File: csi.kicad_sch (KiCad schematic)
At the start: 20 parts, among them J601 Conn_FFC_WE_68712614522_ONE-S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, U601 AP22615A_TSOT26, U602 AP22615A_TSOT26

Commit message: [#53901] Update symbols & footprints from lib
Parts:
- D601, D602: footprint antmicro-footprints:LED_0603_1608Metric_R -> antmicro-footprints:LED_0603_1608Metric_G; symbol antmicroLEDIndicationDiscrete:LED_R_0603_598-8D80-107F -> antmicroLEDIndicationDiscrete:LED_G_0603_598-8D80-107F
- J601: value Conn_FFC_WE_68712614522_ONE-SIDE -> Conn_FFC_WE_68715014522
- TP601, TP602: now left out of the parts list
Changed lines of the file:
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@@
   (title_block
     (title "CM4 Baseboard")
-    (date "2024-03-14")
+    (date "2024-03-22")
     (rev "1.0.0")
     (company "Antmicro")
@@
     )
   )
-  (symbol (lib_id "antmicroLEDIndicationDiscrete:LED_R_0603_598-8D80-107F") (at 152.4 181.61 270) (unit 1)
+  (symbol (lib_id "antmicroLEDIndicationDiscrete:LED_G_0603_598-8D80-107F") (at 152.4 181.61 270) (unit 1)
     (in_bom yes) (on_board yes) (dnp no) (fields_autoplaced)
-    (property "Reference" "D602" (at 157.48 184.4674 90)
+    (property "Reference" "D602" (at 157.48 184.4675 90)
       (effects (font (size 1.27 1.27) (thickness 0.15)) (justify left))
     )
-    (property "Value" "LED_G" (at 157.48 187.0074 90)
+    (property "Value" "LED_G" (at 157.48 187.0075 90)
       (effects (font (size 1.27 1.27) (thickness 0.15)) (justify left))
     )
-    (property "Footprint" "antmicro-footprints:LED_0603_1608Metric_R" (at 144.78 204.47 0)
+    (property "Footprint" "antmicro-footprints:LED_0603_1608Metric_G" (at 144.78 204.47 0)
       (effects (font (size 1.27 1.27) (thickness 0.15)) (justify left bottom) hide)
     )
@@
       (effects (font (size 1.27 1.27) (thickness 0.15)) (justify left bottom) hide)
     )
-    (property "MPN" "598-8D80-107F" (at 157.48 187.0074 90)
-      (effects (font (size 1.27 1.27) (thickness 0.15)) (justify left) hide)
+    (property "MPN" "598-8D80-107F" (at 139.7 204.47 0)
+      (effects (font (size 1.27 1.27) (thickness 0.15)) (justify left bottom) hide)
     )
     (property "Manufacturer" "Dialight" (at 137.16 204.47 0)
@@
     )
     (property "Value" "PESD5Z5_0F" (at 275.59 191.4525 90)
-      (effects (font (size 1.27 1.27) (thickness 0.15)) (justify left))
+      (effects (font (size 1.27 1.27) (thickness 0.15)) (justify left) hide)
     )
     (property "Footprint" "antmicro-footprints:SOD-523" (at 283.21 179.07 0)
@@
       (effects (font (size 1.27 1.27) (thickness 0.15)) (justify left bottom) hide)
     )
-    (property "MPN" "PESD5Z5.0F" (at 290.83 179.07 0)
-      (effects (font (size 1.27 1.27) (thickness 0.15)) (justify left bottom) hide)
+    (property "MPN" "PESD5Z5.0F" (at 275.59 191.4525 90)
+      (effects (font (size 1.27 1.27) (thickness 0.15)) (justify left))
     )
     (property "Author" "Antmicro" (at 293.37 179.07 0)
@@
   )
   (symbol (lib_id "antmicroFCCConnectors:Conn_FFC_WE_68715014522") (at 318.77 62.23 0) (unit 1)
-    (in_bom yes) (on_board yes) (dnp no) (fields_autoplaced)
-    (property "Reference" "J601" (at 323.85 59.69 0)
+    (in_bom yes) (on_board yes) (dnp no)
+    (property "Reference" "J601" (at 318.77 55.88 0)
       (effects (font (size 1.27 1.27)) (justify left))
     )
-    (property "Value" "Conn_FFC_WE_68712614522_ONE-SIDE" (at 325.12 126.9999 0)
+    (property "Value" "Conn_FFC_WE_68715014522" (at 327.66 128.905 0)
       (effects (font (size 1.27 1.27) (thickness 0.15)) (justify left) hide)
     )
@@
       (effects (font (size 1.27 1.27) (thickness 0.15)) (justify left bottom) hide)
     )
-    (property "MPN" "68715014522" (at 328.93 194.31 90)
-      (effects (font (size 1.27 1.27) (thickness 0.15)) (justify left bottom))
+    (property "MPN" "68715014522" (at 318.77 58.42 0)
+      (effects (font (size 1.27 1.27) (thickness 0.15)) (justify left))
     )
     (property "Manufacturer" "Würth Elektronik" (at 337.82 80.01 0)
@@
     )
   )
-  (symbol (lib_id "antmicroLEDIndicationDiscrete:LED_R_0603_598-8D80-107F") (at 152.4 137.16 270) (unit 1)
+  (symbol (lib_id "antmicroLEDIndicationDiscrete:LED_G_0603_598-8D80-107F") (at 152.4 137.16 270) (unit 1)
     (in_bom yes) (on_board yes) (dnp no) (fields_autoplaced)
-    (property "Reference" "D601" (at 157.48 140.0174 90)
+    (property "Reference" "D601" (at 157.48 140.0175 90)
       (effects (font (size 1.27 1.27) (thickness 0.15)) (justify left))
     )
-    (property "Value" "LED_G" (at 157.48 142.5574 90)
+    (property "Value" "LED_G" (at 157.48 142.5575 90)
       (effects (font (size 1.27 1.27) (thickness 0.15)) (justify left))
     )
-    (property "Footprint" "antmicro-footprints:LED_0603_1608Metric_R" (at 144.78 160.02 0)
+    (property "Footprint" "antmicro-footprints:LED_0603_1608Metric_G" (at 144.78 160.02 0)
       (effects (font (size 1.27 1.27) (thickness 0.15)) (justify left bottom) hide)
     )
@@
       (effects (font (size 1.27 1.27) (thickness 0.15)) (justify left bottom) hide)
     )
-    (property "MPN" "598-8D80-107F" (at 157.48 142.5574 90)
-      (effects (font (size 1.27 1.27) (thickness 0.15)) (justify left) hide)
+    (property "MPN" "598-8D80-107F" (at 139.7 160.02 0)
+      (effects (font (size 1.27 1.27) (thickness 0.15)) (justify left bottom) hide)
     )
     (property "Manufacturer" "Dialight" (at 137.16 160.02 0)
@@
     )
     (property "Value" "PESD5Z5_0F" (at 285.75 191.4525 90)
-      (effects (font (size 1.27 1.27) (thickness 0.15)) (justify right))
+      (effects (font (size 1.27 1.27) (thickness 0.15)) (justify right) hide)
     )
     (property "Footprint" "antmicro-footprints:SOD-523" (at 288.29 179.07 0)
@@
       (effects (font (size 1.27 1.27) (thickness 0.15)) (justify left bottom) hide)
     )
-    (property "MPN" "PESD5Z5.0F" (at 295.91 179.07 0)
-      (effects (font (size 1.27 1.27) (thickness 0.15)) (justify left bottom) hide)
+    (property "MPN" "PESD5Z5.0F" (at 285.75 191.4525 90)
+      (effects (font (size 1.27 1.27) (thickness 0.15)) (justify right))
     )
     (property "Author" "Antmicro" (at 298.45 179.07 0)
@@
   )
   (symbol (lib_id "antmicroTestPoints:TP_0.75mm_SMD") (at 116.84 176.53 0) (mirror y) (unit 1)
-    (in_bom yes) (on_board yes) (dnp no) (fields_autoplaced)
+    (in_bom no) (on_board yes) (dnp no) (fields_autoplaced)
     (property "Reference" "TP602" (at 111.76 176.5299 0)
       (effects (font (size 1.27 1.27)) (justify left))
@@
   )
   (symbol (lib_id "antmicroTestPoints:TP_0.75mm_SMD") (at 116.84 132.08 0) (mirror y) (unit 1)
-    (in_bom yes) (on_board yes) (dnp no) (fields_autoplaced)
+    (in_bom no) (on_board yes) (dnp no) (fields_autoplaced)
     (property "Reference" "TP601" (at 111.76 132.0799 0)
       (effects (font (size 1.27 1.27)) (justify left))

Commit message: [#56708] Add loclib
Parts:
- C601, C602: footprint antmicro-footprints:C_0402_1005Metric -> cm4-baseboard-footprints:C_0402_1005Metric; symbol antmicroCapacitors0402:C_100n_0402 -> cm4-baseboard:C_100n_0402
- C603, C604: footprint antmicro-footprints:C_0402_1005Metric -> cm4-baseboard-footprints:C_0402_1005Metric; symbol antmicroCapacitors0402:C_1u_0402 -> cm4-baseboard:C_1u_0402
- D601, D602: footprint antmicro-footprints:LED_0603_1608Metric_G -> cm4-baseboard-footprints:LED_0603_1608Metric_G; symbol antmicroLEDIndicationDiscrete:LED_G_0603_598-8D80-107F -> cm4-baseboard:LED_G_0603_598-8D80-107F
- D603, D604: footprint antmicro-footprints:SOD-523 -> cm4-baseboard-footprints:SOD-523; symbol antmicroTVSDiodes:PESD5Z5_0F -> cm4-baseboard:PESD5Z5_0F
- J601: footprint antmicro-footprints:Conn_FFC_WE_68715014x22 -> cm4-baseboard-footprints:Conn_FFC_WE_68715014x22; symbol antmicroFCCConnectors:Conn_FFC_WE_68715014522 -> cm4-baseboard:Conn_FFC_WE_68715014522
- R601: footprint antmicro-footprints:R_0402_1005Metric -> cm4-baseboard-footprints:R_0402_1005Metric; symbol antmicroResistors0402:R_100k_0402 -> cm4-baseboard:R_100k_0402
- R602, R603: footprint antmicro-footprints:R_0402_1005Metric -> cm4-baseboard-footprints:R_0402_1005Metric; symbol antmicroResistors0402:R_10k_0402 -> cm4-baseboard:R_10k_0402
- R604, R605: footprint antmicro-footprints:R_0402_1005Metric -> cm4-baseboard-footprints:R_0402_1005Metric; symbol antmicroResistors0402:R_4k7_0402 -> cm4-baseboard:R_4k7_0402
- R606: footprint antmicro-footprints:R_0402_1005Metric -> cm4-baseboard-footprints:R_0402_1005Metric; symbol antmicroResistors0402:R_470R_0402 -> cm4-baseboard:R_470R_0402
- R607: footprint antmicro-footprints:R_0402_1005Metric -> cm4-baseboard-footprints:R_0402_1005Metric; symbol antmicroResistors0402:R_200R_0402 -> cm4-baseboard:R_200R_0402
- TP601, TP602: footprint antmicro-footprints:TP_SMD_0.75mm -> cm4-baseboard-footprints:TP_SMD_0.75mm; symbol antmicroTestPoints:TP_0.75mm_SMD -> cm4-baseboard:TP_0.75mm_SMD
- U601, U602: footprint antmicro-footprints:TSOT23-6 -> cm4-baseboard-footprints:TSOT23-6; symbol antmicroPMICPowerDistributionSwitchesLoadDrivers:AP22615A_TSOT26 -> cm4-baseboard:AP22615A_TSOT26

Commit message: [#56708] Update symbol/footprint props; Update modules visibilty
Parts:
- D601, D602: value LED_G -> LED_G_0603_598-8D80-107F; Color (none) -> Green
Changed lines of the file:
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@@
     (comment 1 "www.antmicro.com")
   )
+  (bus_alias "CamCtrl" (members "EN" "VSYNC0" "VSYNC1"))
   (junction (at 152.4 173.99) (diameter 0) (color 0 0 0 0)
   )
@@
     (stroke (width 0) (type default))
   )
-  (bus_alias "CamCtrl" (members "EN" "VSYNC0" "VSYNC1"))
   (bus (pts (xy 295.91 74.93) (xy 295.91 77.47))
     (stroke (width 0) (type default))
@@
       (effects (font (size 1.27 1.27) (thickness 0.15)) (justify left))
     )
-    (property "Value" "LED_G" (at 157.48 187.0075 90)
-      (effects (font (size 1.27 1.27) (thickness 0.15)) (justify left))
+    (property "Value" "LED_G_0603_598-8D80-107F" (at 144.78 204.47 0)
+      (effects (font (size 1.27 1.27) (thickness 0.15)) (justify left bottom) hide)
     )
-    (property "Footprint" "cm4-baseboard-footprints:LED_0603_1608Metric_G" (at 144.78 204.47 0)
+    (property "Footprint" "cm4-baseboard-footprints:LED_0603_1608Metric_G" (at 142.24 204.47 0)
       (effects (font (size 1.27 1.27) (thickness 0.15)) (justify left bottom) hide)
     )
-    (property "Datasheet" "https://www.farnell.com/datasheets/3093797.pdf" (at 142.24 204.47 0)
+    (property "Datasheet" "https://www.farnell.com/datasheets/3093797.pdf" (at 139.7 204.47 0)
       (effects (font (size 1.27 1.27) (thickness 0.15)) (justify left bottom) hide)
     )
-    (property "MPN" "598-8D80-107F" (at 139.7 204.47 0)
+    (property "MPN" "598-8D80-107F" (at 137.16 204.47 0)
       (effects (font (size 1.27 1.27) (thickness 0.15)) (justify left bottom) hide)
     )
-    (property "Manufacturer" "Dialight" (at 137.16 204.47 0)
+    (property "Manufacturer" "Dialight" (at 134.62 204.47 0)
       (effects (font (size 1.27 1.27) (thickness 0.15)) (justify left bottom) hide)
     )
-    (property "Author" "Antmicro" (at 134.62 204.47 0)
+    (property "Author" "Antmicro" (at 132.08 204.47 0)
       (effects (font (size 1.27 1.27) (thickness 0.15)) (justify left bottom) hide)
     )
-    (property "License" "Apache-2.0" (at 132.08 204.47 0)
+    (property "License" "Apache-2.0" (at 129.54 204.47 0)
       (effects (font (size 1.27 1.27) (thickness 0.15)) (justify left bottom) hide)
     )
+    (property "Color" "Green" (at 157.48 187.0075 90)
+      (effects (font (size 1.27 1.27)) (justify left))
+    )
     (pin "1")
     (pin "2")
@@
       (effects (font (size 1.27 1.27) (thickness 0.15)) (justify left))
     )
-    (property "Value" "LED_G" (at 157.48 142.5575 90)
-      (effects (font (size 1.27 1.27) (thickness 0.15)) (justify left))
+    (property "Value" "LED_G_0603_598-8D80-107F" (at 144.78 160.02 0)
+      (effects (font (size 1.27 1.27) (thickness 0.15)) (justify left bottom) hide)
     )
-    (property "Footprint" "cm4-baseboard-footprints:LED_0603_1608Metric_G" (at 144.78 160.02 0)
+    (property "Footprint" "cm4-baseboard-footprints:LED_0603_1608Metric_G" (at 142.24 160.02 0)
       (effects (font (size 1.27 1.27) (thickness 0.15)) (justify left bottom) hide)
     )
-    (property "Datasheet" "https://www.farnell.com/datasheets/3093797.pdf" (at 142.24 160.02 0)
+    (property "Datasheet" "https://www.farnell.com/datasheets/3093797.pdf" (at 139.7 160.02 0)
       (effects (font (size 1.27 1.27) (thickness 0.15)) (justify left bottom) hide)
     )
-    (property "MPN" "598-8D80-107F" (at 139.7 160.02 0)
+    (property "MPN" "598-8D80-107F" (at 137.16 160.02 0)
       (effects (font (size 1.27 1.27) (thickness 0.15)) (justify left bottom) hide)
     )
-    (property "Manufacturer" "Dialight" (at 137.16 160.02 0)
+    (property "Manufacturer" "Dialight" (at 134.62 160.02 0)
       (effects (font (size 1.27 1.27) (thickness 0.15)) (justify left bottom) hide)
     )
-    (property "Author" "Antmicro" (at 134.62 160.02 0)
+    (property "Author" "Antmicro" (at 132.08 160.02 0)
       (effects (font (size 1.27 1.27) (thickness 0.15)) (justify left bottom) hide)
     )
-    (property "License" "Apache-2.0" (at 132.08 160.02 0)
+    (property "License" "Apache-2.0" (at 129.54 160.02 0)
       (effects (font (size 1.27 1.27) (thickness 0.15)) (justify left bottom) hide)
     )
+    (property "Color" "Green" (at 157.48 142.5575 90)
+      (effects (font (size 1.27 1.27)) (justify left))
+    )
     (pin "1")

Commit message: [#57456] Remove loclib
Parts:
- C601, C602: footprint cm4-baseboard-footprints:C_0402_1005Metric -> antmicro-footprints:C_0402_1005Metric; symbol cm4-baseboard:C_100n_0402 -> antmicroCapacitors0402:C_100n_0402
- C603, C604: footprint cm4-baseboard-footprints:C_0402_1005Metric -> antmicro-footprints:C_0402_1005Metric; symbol cm4-baseboard:C_1u_0402 -> antmicroCapacitors0402:C_1u_0402
- D601, D602: footprint cm4-baseboard-footprints:LED_0603_1608Metric_G -> antmicro-footprints:LED_0603_1608Metric_G; symbol cm4-baseboard:LED_G_0603_598-8D80-107F -> antmicroLEDIndicationDiscrete:LED_G_0603_598-8D80-107F
- D603, D604: footprint cm4-baseboard-footprints:SOD-523 -> antmicro-footprints:SOD-523; symbol cm4-baseboard:PESD5Z5_0F -> antmicroTVSDiodes:PESD5Z5_0F
- J601: footprint cm4-baseboard-footprints:Conn_FFC_WE_68715014x22 -> antmicro-footprints:Conn_FFC_WE_68715014x22; symbol cm4-baseboard:Conn_FFC_WE_68715014522 -> antmicroFCCConnectors:Conn_FFC_WE_68715014522
- R601: footprint cm4-baseboard-footprints:R_0402_1005Metric -> antmicro-footprints:R_0402_1005Metric; symbol cm4-baseboard:R_100k_0402 -> antmicroResistors0402:R_100k_0402
- R602, R603: footprint cm4-baseboard-footprints:R_0402_1005Metric -> antmicro-footprints:R_0402_1005Metric; symbol cm4-baseboard:R_10k_0402 -> antmicroResistors0402:R_10k_0402
- R604, R605: footprint cm4-baseboard-footprints:R_0402_1005Metric -> antmicro-footprints:R_0402_1005Metric; symbol cm4-baseboard:R_4k7_0402 -> antmicroResistors0402:R_4k7_0402
- R606: footprint cm4-baseboard-footprints:R_0402_1005Metric -> antmicro-footprints:R_0402_1005Metric; symbol cm4-baseboard:R_470R_0402 -> antmicroResistors0402:R_470R_0402
- R607: footprint cm4-baseboard-footprints:R_0402_1005Metric -> antmicro-footprints:R_0402_1005Metric; symbol cm4-baseboard:R_200R_0402 -> antmicroResistors0402:R_200R_0402
- TP601, TP602: footprint cm4-baseboard-footprints:TP_SMD_0.75mm -> antmicro-footprints:TP_SMD_0.75mm; symbol cm4-baseboard:TP_0.75mm_SMD -> antmicroTestPoints:TP_0.75mm_SMD
- U601, U602: footprint cm4-baseboard-footprints:TSOT23-6 -> antmicro-footprints:TSOT23-6; symbol cm4-baseboard:AP22615A_TSOT26 -> antmicroPMICPowerDistributionSwitchesLoadDrivers:AP22615A_TSOT26

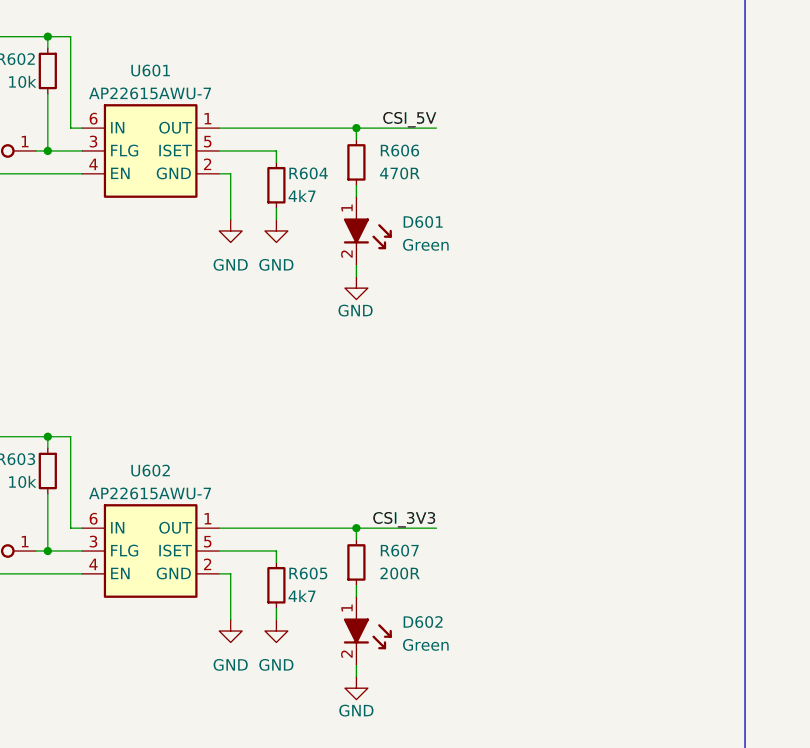
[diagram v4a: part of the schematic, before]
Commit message: [#58122] LED related fixes & improvements
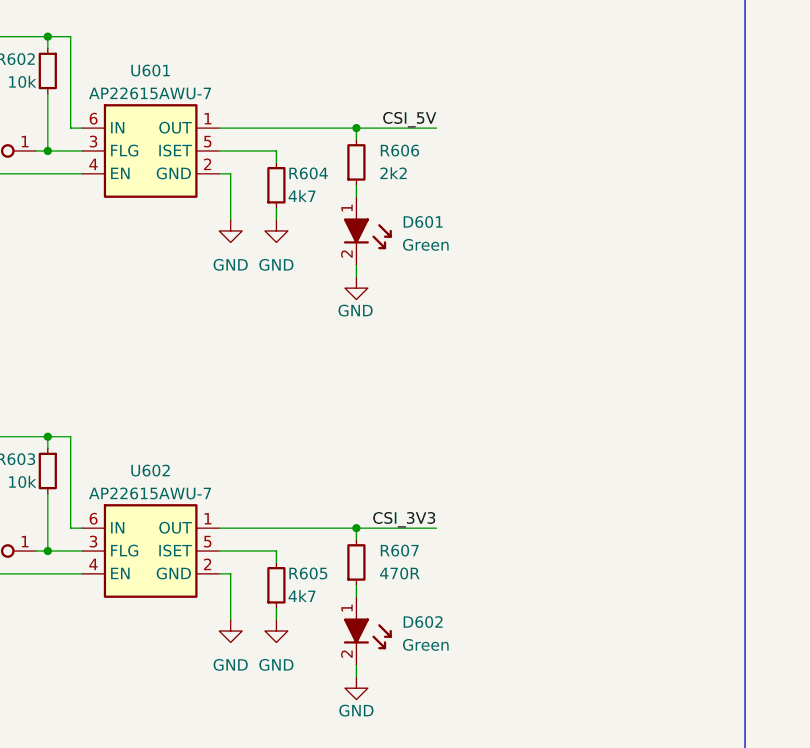
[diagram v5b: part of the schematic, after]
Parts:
- R606: value R_470R_0402 -> R_2k2_0402; symbol antmicroResistors0402:R_470R_0402 -> antmicroResistors0402:R_2k2_0402; MPN CR0402-FX-4700GLF -> CR0402-FX-2201GLF; Val 470R -> 2k2
- R607: value R_200R_0402 -> R_470R_0402; symbol antmicroResistors0402:R_200R_0402 -> antmicroResistors0402:R_470R_0402; MPN CR0402-FX-2000GLF -> CR0402-FX-4700GLF; Val 200R -> 470R
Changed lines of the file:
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@@
     )
   )
-  (symbol (lib_id "antmicroResistors0402:R_470R_0402") (at 152.4 135.89 90) (unit 1)
+  (symbol (lib_id "antmicroResistors0402:R_2k2_0402") (at 152.4 135.89 90) (unit 1)
     (in_bom yes) (on_board yes) (dnp no) (fields_autoplaced)
     (property "Reference" "R606" (at 154.94 132.0799 90)
       (effects (font (size 1.27 1.27)) (justify right))
     )
-    (property "Value" "R_470R_0402" (at 165.1 115.57 0)
+    (property "Value" "R_2k2_0402" (at 165.1 115.57 0)
       (effects (font (size 1.27 1.27) (thickness 0.15)) (justify left bottom) hide)
     )
@@
       (effects (font (size 1.27 1.27) (thickness 0.15)) (justify left bottom) hide)
     )
-    (property "MPN" "CR0402-FX-4700GLF" (at 172.72 115.57 0)
+    (property "MPN" "CR0402-FX-2201GLF" (at 172.72 115.57 0)
       (effects (font (size 1.27 1.27) (thickness 0.15)) (justify left bottom) hide)
     )
-    (property "Val" "470R" (at 154.94 134.6199 90)
+    (property "Val" "2k2" (at 154.94 134.6199 90)
       (effects (font (size 1.27 1.27) (thickness 0.15)) (justify right))
     )
@@
     )
   )
-  (symbol (lib_id "antmicroResistors0402:R_200R_0402") (at 152.4 180.34 90) (unit 1)
+  (symbol (lib_id "antmicroResistors0402:R_470R_0402") (at 152.4 180.34 90) (unit 1)
     (in_bom yes) (on_board yes) (dnp no) (fields_autoplaced)
     (property "Reference" "R607" (at 154.94 176.5299 90)
       (effects (font (size 1.27 1.27)) (justify right))
     )
-    (property "Value" "R_200R_0402" (at 165.1 160.02 0)
+    (property "Value" "R_470R_0402" (at 165.1 160.02 0)
       (effects (font (size 1.27 1.27) (thickness 0.15)) (justify left bottom) hide)
     )
@@
       (effects (font (size 1.27 1.27) (thickness 0.15)) (justify left bottom) hide)
     )
-    (property "MPN" "CR0402-FX-2000GLF" (at 172.72 160.02 0)
+    (property "MPN" "CR0402-FX-4700GLF" (at 172.72 160.02 0)
       (effects (font (size 1.27 1.27) (thickness 0.15)) (justify left bottom) hide)
     )
-    (property "Val" "200R" (at 154.94 179.0699 90)
+    (property "Val" "470R" (at 154.94 179.0699 90)
       (effects (font (size 1.27 1.27) (thickness 0.15)) (justify right))
     )
